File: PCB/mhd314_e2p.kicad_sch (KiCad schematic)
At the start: 10 parts, among them U10 AT24CS64-SSHM

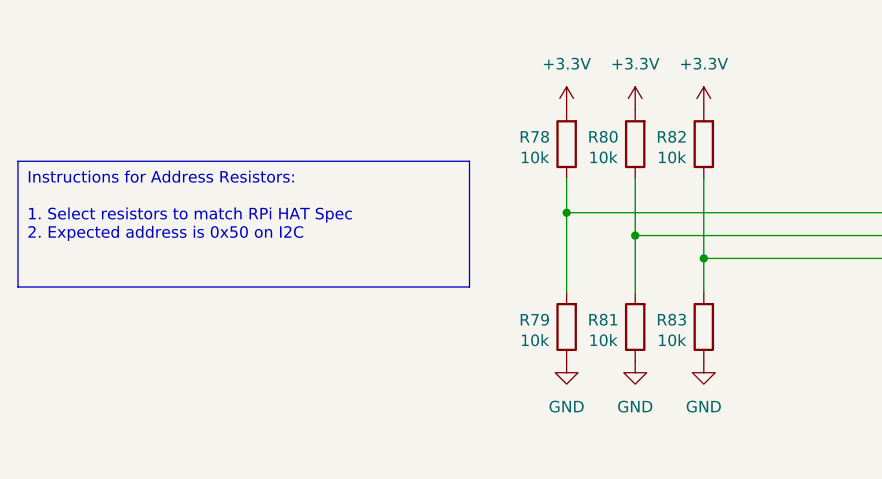
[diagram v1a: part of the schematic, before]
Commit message: Routing revised, added some missing parameters to components
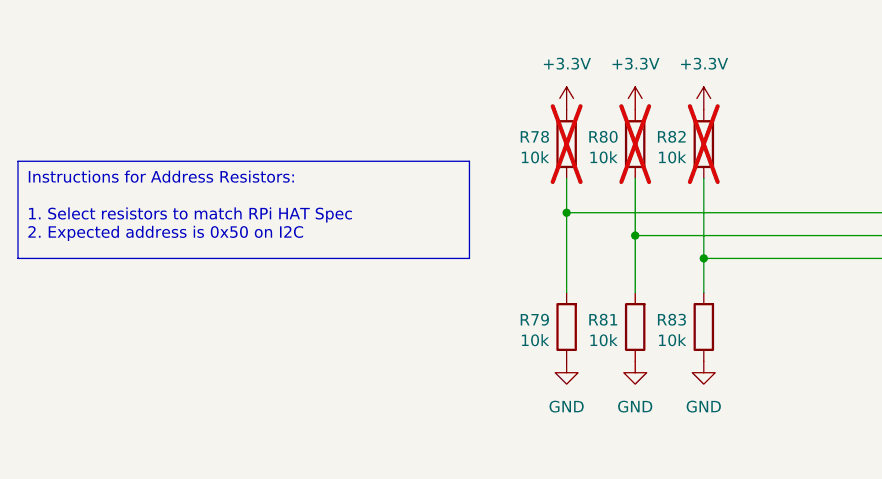
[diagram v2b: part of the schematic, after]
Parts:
- R78, R80, R82: now not fitted
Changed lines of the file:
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@@
 		(exclude_from_sim no)
 		(at 34.29 90.805 0)
-		(size 50.165 13.97)
+		(size 50.165 10.795)
 		(stroke
 			(width 0)
@@
 		(in_bom yes)
 		(on_board yes)
-		(dnp no)
+		(dnp yes)
 		(property "Reference" "R82"
 			(at 106.934 88.138 0)
@@
 		(in_bom yes)
 		(on_board yes)
-		(dnp no)
+		(dnp yes)
 		(property "Reference" "R78"
 			(at 91.694 88.138 0)
@@
 		(in_bom yes)
 		(on_board yes)
-		(dnp no)
+		(dnp yes)
 		(property "Reference" "R80"
 			(at 99.314 88.138 0)

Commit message: Updated PCB with digital traxce suggestions. Added JLCPCB Pns
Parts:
- C31: JLCPCBPn (none) -> C1525; Voltage 25V -> 16V
- R79, R81, R83: JLCPCBPn (none) -> C25744
- R84, R85: JLCPCBPn (none) -> C4109
- U10: JLCPCBPn (none) -> C615478
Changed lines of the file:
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@@
 			)
 		)
-		(property "Voltage" "25V"
+		(property "Voltage" "16V"
+			(at 140.97 137.16 0)
+			(effects
+				(font
+					(size 1.27 1.27)
+				)
+				(hide yes)
+			)
+		)
+		(property "JLCPCBPn" "C1525"
 			(at 140.97 137.16 0)
 			(effects
@@
 			)
 		)
+		(property "JLCPCBPn" "C25744"
+			(at 102.87 109.22 0)
+			(effects
+				(font
+					(size 1.27 1.27)
+				)
+				(hide yes)
+			)
+		)
 		(pin "2"
 		)
@@
 			)
 		)
+		(property "JLCPCBPn" "C615478"
+			(at 142.24 99.06 0)
+			(effects
+				(font
+					(size 1.27 1.27)
+				)
+				(hide yes)
+			)
+		)
 		(pin "1"
 		)
@@
 			)
 		)
+		(property "JLCPCBPn" "C25744"
+			(at 95.25 109.22 0)
+			(effects
+				(font
+					(size 1.27 1.27)
+				)
+				(hide yes)
+			)
+		)
 		(pin "2"
 		)
@@
 			)
 		)
+		(property "JLCPCBPn" "C25744"
+			(at 110.49 109.22 0)
+			(effects
+				(font
+					(size 1.27 1.27)
+				)
+				(hide yes)
+			)
+		)
 		(pin "2"
 		)
@@
 			)
 		)
+		(property "JLCPCBPn" "C4109"
+			(at 170.18 88.9 0)
+			(effects
+				(font
+					(size 1.27 1.27)
+				)
+				(hide yes)
+			)
+		)
 		(pin "2"
 		)
@@
 			(at 177.8 88.9 0)
 			(effects
+				(font
+					(size 1.27 1.27)
+				)
+				(hide yes)
+			)
+		)
+		(property "JLCPCBPn" "C4109"
+			(at 177.8 88.9 0)
+			(effects

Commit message: Added filter capacitors to OPA1622 circuitry
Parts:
- C31: JLCPCBPn C1525 -> (none); LCSC Part # (none) -> C1525
- R79, R81, R83: JLCPCBPn C25744 -> (none); LCSC Part # (none) -> C25744
- R84, R85: JLCPCBPn C4109 -> (none); LCSC Part # (none) -> C4109
- U10: JLCPCBPn C615478 -> (none); LCSC Part # (none) -> C615478
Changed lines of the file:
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@@
 			)
 		)
-		(property "JLCPCBPn" "C1525"
+		(property "LCSC Part #" "C1525"
 			(at 140.97 137.16 0)
 			(effects
@@
 			)
 		)
-		(property "JLCPCBPn" "C25744"
+		(property "LCSC Part #" "C25744"
 			(at 102.87 109.22 0)
 			(effects
@@
 			)
 		)
-		(property "JLCPCBPn" "C615478"
+		(property "LCSC Part #" "C615478"
 			(at 142.24 99.06 0)
 			(effects
@@
 			)
 		)
-		(property "JLCPCBPn" "C25744"
+		(property "LCSC Part #" "C25744"
 			(at 95.25 109.22 0)
 			(effects
@@
 			)
 		)
-		(property "JLCPCBPn" "C25744"
+		(property "LCSC Part #" "C25744"
 			(at 110.49 109.22 0)
 			(effects
@@
 			)
 		)
-		(property "JLCPCBPn" "C4109"
+		(property "LCSC Part #" "C4109"
 			(at 170.18 88.9 0)
 			(effects
@@
 			)
 		)
-		(property "JLCPCBPn" "C4109"
+		(property "LCSC Part #" "C4109"
 			(at 177.8 88.9 0)
 			(effects

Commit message: Changed the BOM field for JLCPCB to the original name instead of LCSC
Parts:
- C31: JLCPCB Part # (none) -> C1525; LCSC Part # C1525 -> (none)
- R79, R81, R83: JLCPCB Part # (none) -> C25744; LCSC Part # C25744 -> (none)
- R84, R85: JLCPCB Part # (none) -> C4109; LCSC Part # C4109 -> (none)
- U10: JLCPCB Part # (none) -> C615478; LCSC Part # C615478 -> (none)
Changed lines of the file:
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@@
 			)
 		)
-		(property "LCSC Part #" "C1525"
+		(property "JLCPCB Part #" "C1525"
 			(at 140.97 137.16 0)
 			(effects
@@
 			)
 		)
-		(property "LCSC Part #" "C25744"
+		(property "JLCPCB Part #" "C25744"
 			(at 102.87 109.22 0)
 			(effects
@@
 			)
 		)
-		(property "LCSC Part #" "C615478"
+		(property "JLCPCB Part #" "C615478"
 			(at 142.24 99.06 0)
 			(effects
@@
 			)
 		)
-		(property "LCSC Part #" "C25744"
+		(property "JLCPCB Part #" "C25744"
 			(at 95.25 109.22 0)
 			(effects
@@
 			)
 		)
-		(property "LCSC Part #" "C25744"
+		(property "JLCPCB Part #" "C25744"
 			(at 110.49 109.22 0)
 			(effects
@@
 			)
 		)
-		(property "LCSC Part #" "C4109"
+		(property "JLCPCB Part #" "C4109"
 			(at 170.18 88.9 0)
 			(effects
@@
 			)
 		)
-		(property "LCSC Part #" "C4109"
+		(property "JLCPCB Part #" "C4109"
 			(at 177.8 88.9 0)
 			(effects

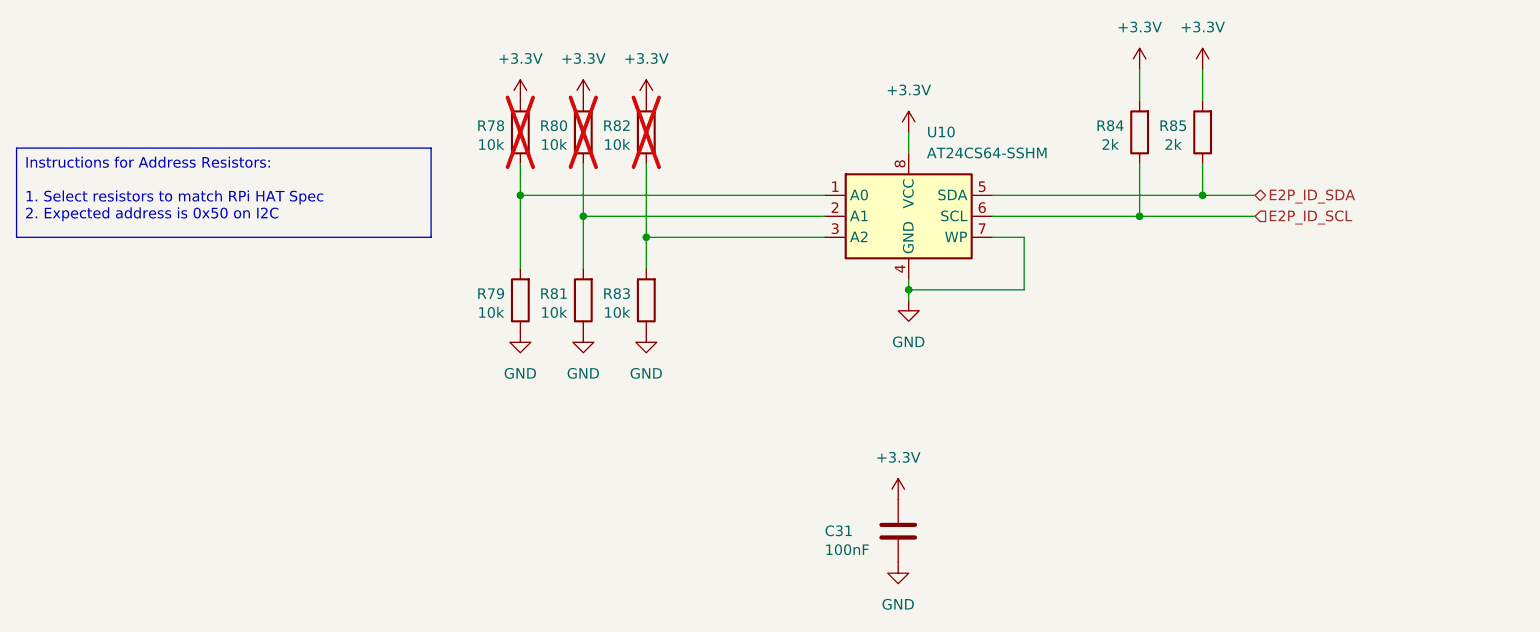
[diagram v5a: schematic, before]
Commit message: Changes in E2P for better identification of the board
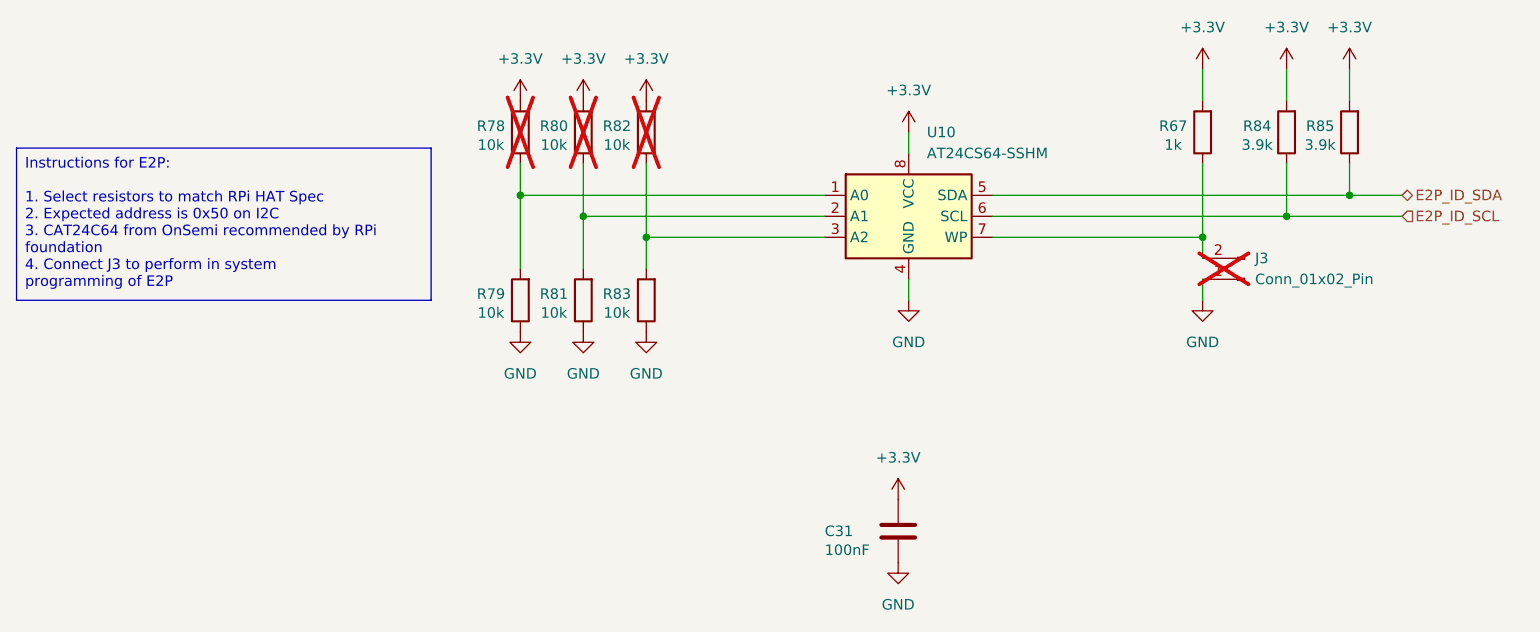
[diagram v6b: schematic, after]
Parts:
- added J3: Conn_01x02_Pin, Connector_PinHeader_1.00mm:PinHeader_1x02_P1.00mm_Vertical, symbol Connector:Conn_01x02_Pin
- added R67: 1k, Resistor_SMD:R_0402_1005Metric_Pad0.72x0.64mm_HandSolder, symbol Device:R
- R84, R85: value 2k -> 3.9k; JLCPCB Part # C4109 -> C51721
- U10: JLCPCB Part # C615478 -> C81193
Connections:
- net +3.3V: now also R67.2
- net GND: now also J3.1 (Pin_1); no longer U10.7 (WP)
- new net: J3.2 (Pin_2), R67.1, U10.7 (WP)
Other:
- moved on the sheet: R84, R85
